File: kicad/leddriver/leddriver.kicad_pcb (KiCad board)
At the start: 2 copper layers, 63.6 x 41.1 mm, 18 parts, among them J1 Conn_01x01_Male, J2 Conn_01x02_Male, Q1 2N3904, SW1 SW_Push, U1 TLC555xP, U2 TLC555xP

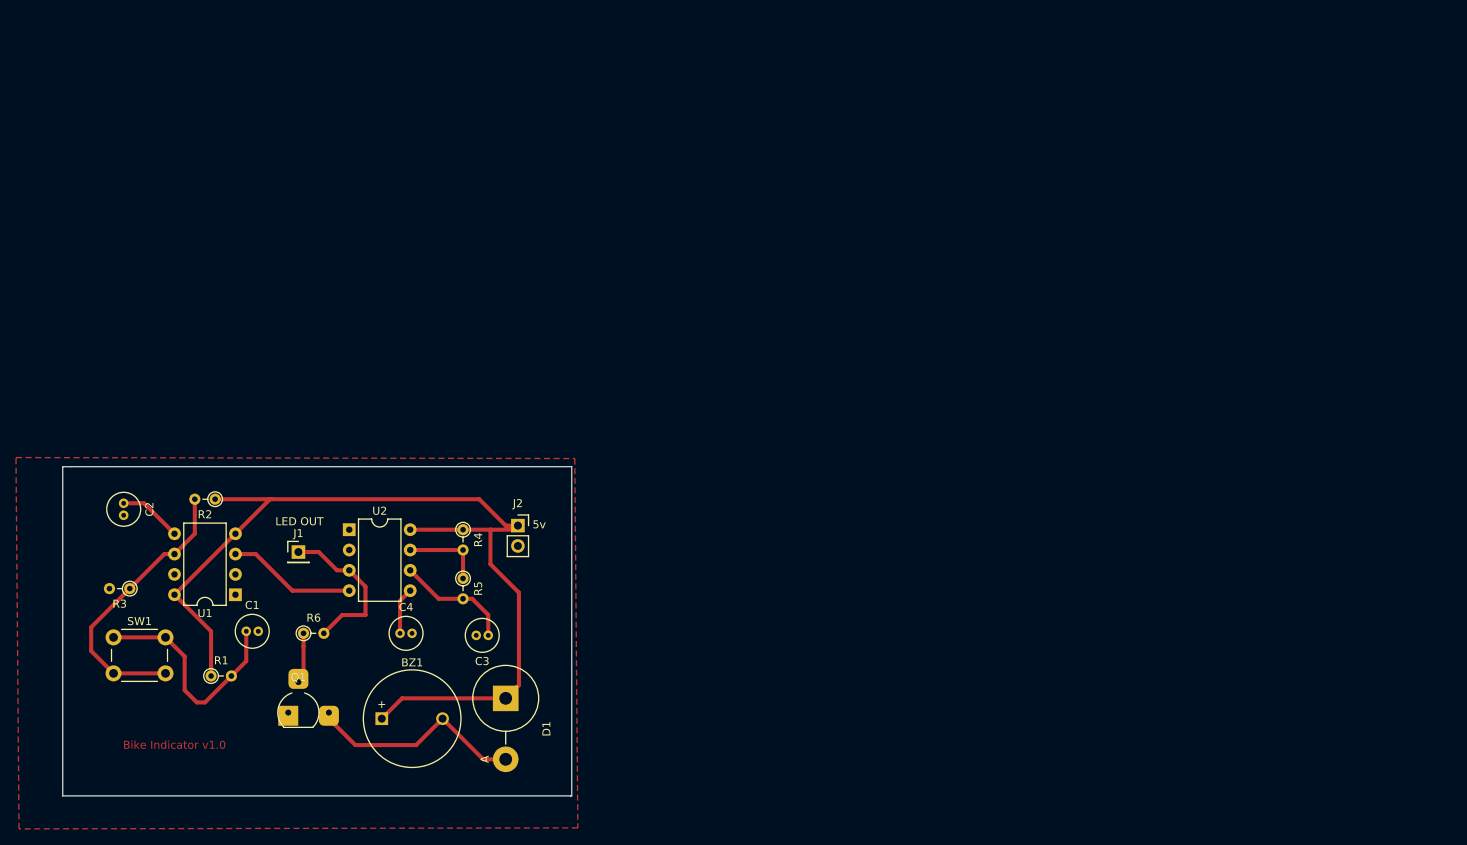
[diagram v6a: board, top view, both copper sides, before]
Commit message: Add bigger pads and track
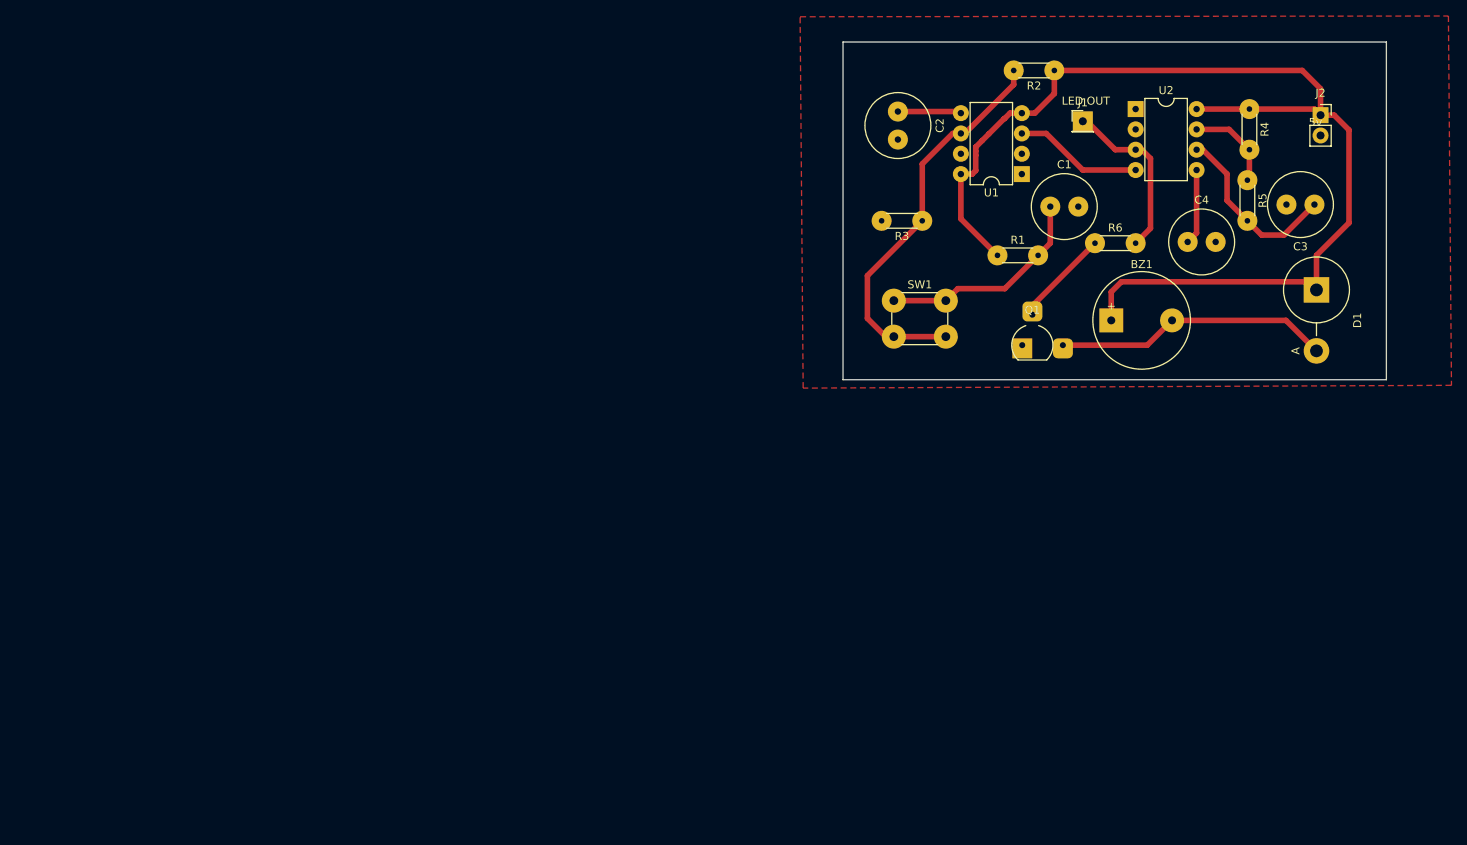
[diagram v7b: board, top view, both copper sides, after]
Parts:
- C1, C2, C3, C4: footprint Capacitor_THT:C_Radial_D4.0mm_H5.0mm_P1.50mm -> Capacitor_THT:C_Radial_D8.0mm_H7.0mm_P3.50mm
- R1, R2, R3, R4, R5, R6: footprint Resistor_THT:R_Axial_DIN0204_L3.6mm_D1.6mm_P2.54mm_Vertical -> Resistor_THT:R_Axial_DIN0204_L3.6mm_D1.6mm_P5.08mm_Horizontal
- moved R2 117.8 mm to (242.3, 19.8)
- moved C3 116.5 mm to (274.8, 36.6)
- moved C1 113.7 mm to (241.8, 36.8)
- moved D1 113.5 mm to (275.1, 47.2)
- moved J2 112.7 mm to (275.6, 25.4)
- moved J1 111.9 mm to (245.9, 26.2)
- moved R1 111.5 mm to (235.2, 42.9)
- moved R4 111.5 mm to (266.7, 24.6)
- moved U1 111.5 mm to (238.3, 32.8)
- moved U2 111.5 mm to (252.5, 24.6)
- moved R6 110.3 mm to (247.4, 41.4)
- moved R5 110.0 mm to (266.4, 33.5)
- moved C4 109.9 mm to (259.0, 41.2)
- moved R3 109.2 mm to (225.8, 38.6)
- moved C2 108.5 mm to (222.8, 24.9)
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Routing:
- net VCC: track 122.5 -> 142.0 mm
- net /THR1: track 35.5 -> 50.2 mm
- net /THR2: track 14.6 -> 22.7 mm
- net Net-(BZ1-Pad2): track 27.7 -> 34.6 mm
- net Net-(Q1-Pad2): track 6.36 -> 12.2 mm
- net /CTRL2: track 5.86 -> 9.45 mm
- net OUT: track 19.9 -> 21.7 mm
- net /DIS2: track 10.2 -> 11.6 mm
- net Net-(C1-Pad1): track 28.3 -> 27.1 mm
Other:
- board size 63.6 x 41.1 mm -> 67.9 x 42.2 mm
- net class homemade2 added: clearance 0.508, trace_width 0.7, via_dia 0.8, via_drill 0.4
- board text removed: "Bike Indicator v1.0"

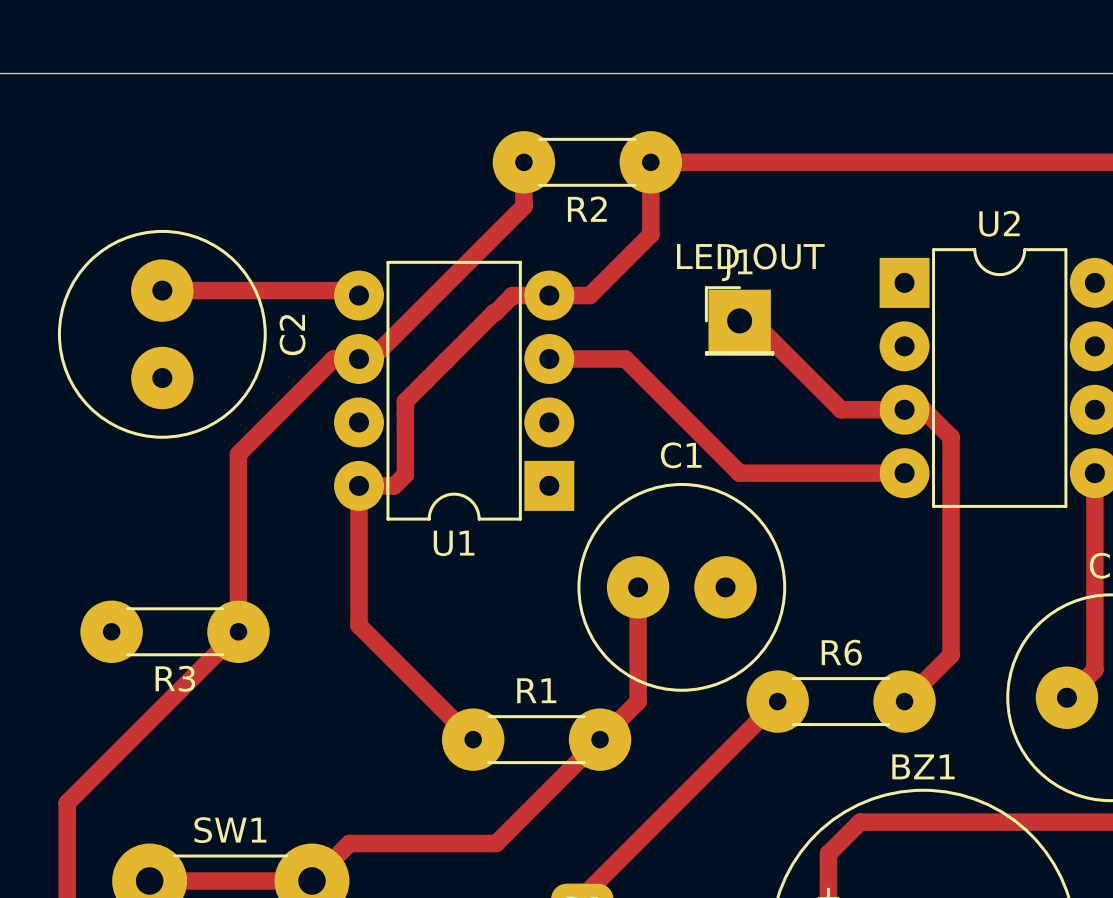
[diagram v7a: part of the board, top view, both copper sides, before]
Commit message: Add new led driver
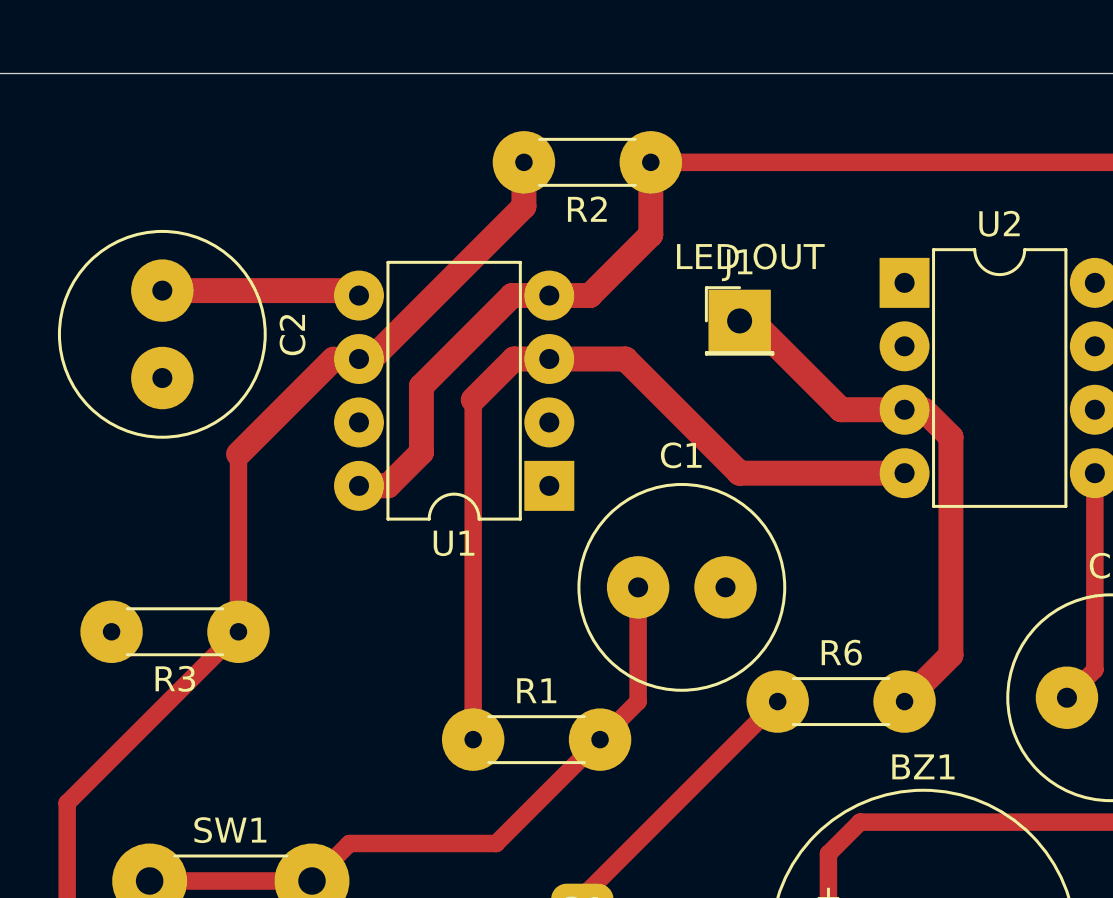
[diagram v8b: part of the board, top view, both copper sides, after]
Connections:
- R1 pad 1: VCC -> OUT1
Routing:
- net OUT1: track 16.1 -> 33.4 mm
- net VCC: track 142.0 -> 129.8 mm
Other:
- net class homemade2: clearance 0.508 -> 0.7
- net class homemade3 added: clearance 1, trace_width 1, via_dia 0.8, via_drill 0.4
